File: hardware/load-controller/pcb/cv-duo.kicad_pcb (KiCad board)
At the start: 2 copper layers, 77.8 x 60.4 mm, 43 parts, among them J1 USB-C 16P receptacle, J2 5V DC input, J3 Relay load out (mains), J4 Pulse output, K1 Omron G5Q-1A 5VDC, Q1 AO3400A, Q2 AO3400A, SW1 RESET tactile, SW2 BOOT tactile, U1 ESP32-C3-WROOM-02 (4MB), U2 AP2112K-3.3, U3 USBLC6-2SC6

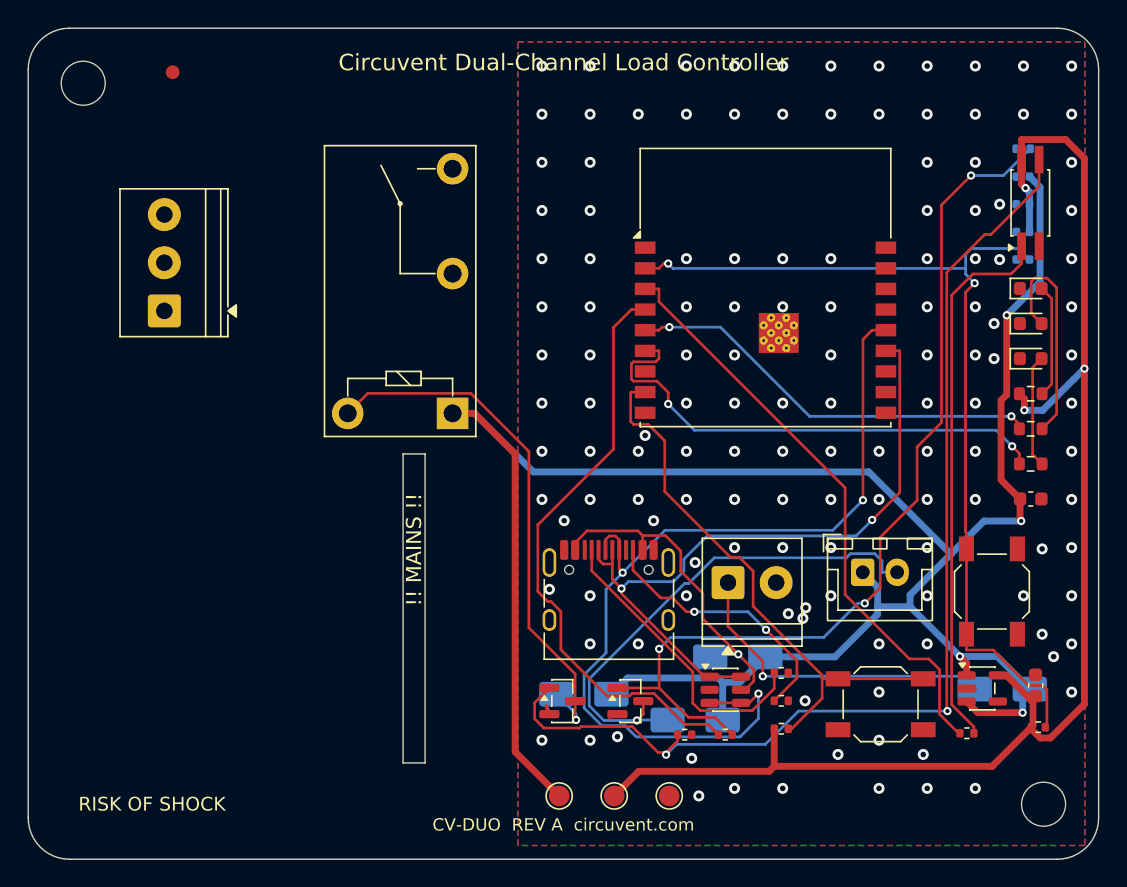
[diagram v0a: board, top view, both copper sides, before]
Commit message: Release 1.10.0, and stop shipping permissions the app never uses
Cut 1.10.0 (versionCode 12) and built it: AAB 38 MB, APK 83 MB, signed with the
upload key, JS bundle embedded.

Checking the generated manifest before writing the Play listing turned up
permissions no one had asked for. Every one of them is printed on the store page
for users to read before they install:

  RECORD_AUDIO          expo-camera asks for the microphone so video can be
                        recorded with sound. This app only ever puts the camera
                        in barcode mode to read a QR label, and expo-speech is
                        output-only - it speaks, it does not listen. Left in,
                        Play lists "Microphone" against a home-control app,
                        which is alarming, unexplainable and untrue.
  SYSTEM_ALERT_WINDOW   React Native's development overlay, useless in a release
                        build and shown to users as "Display over other apps".
  READ/WRITE_EXTERNAL_STORAGE
                        Legacy storage access nothing here touches.

Stripped via android.blockedPermissions. That emits tools:node="remove", which
is a merge instruction rather than a guarantee, so it was checked against the
finished artifact with aapt2 rather than the source manifest - all four are
absent from the APK.

NEARBY_WIFI_DEVICES now carries neverForLocation. Android otherwise treats it as
location-capable, because knowing which networks are in range is enough to place
someone, and Play's data safety review treats it the same way. The app uses it
only to join a new device's setup hotspot. That flag is a promise, so the plugin
says plainly that it has to come off if scan results are ever used positionally.

What is left is defensible: location for Wi-Fi onboarding (Android requires it),
camera for the QR label, nearby-devices flagged as non-positional.

Added mobile/store/listing with the text Play asks for - title, short and full
descriptions, and what'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
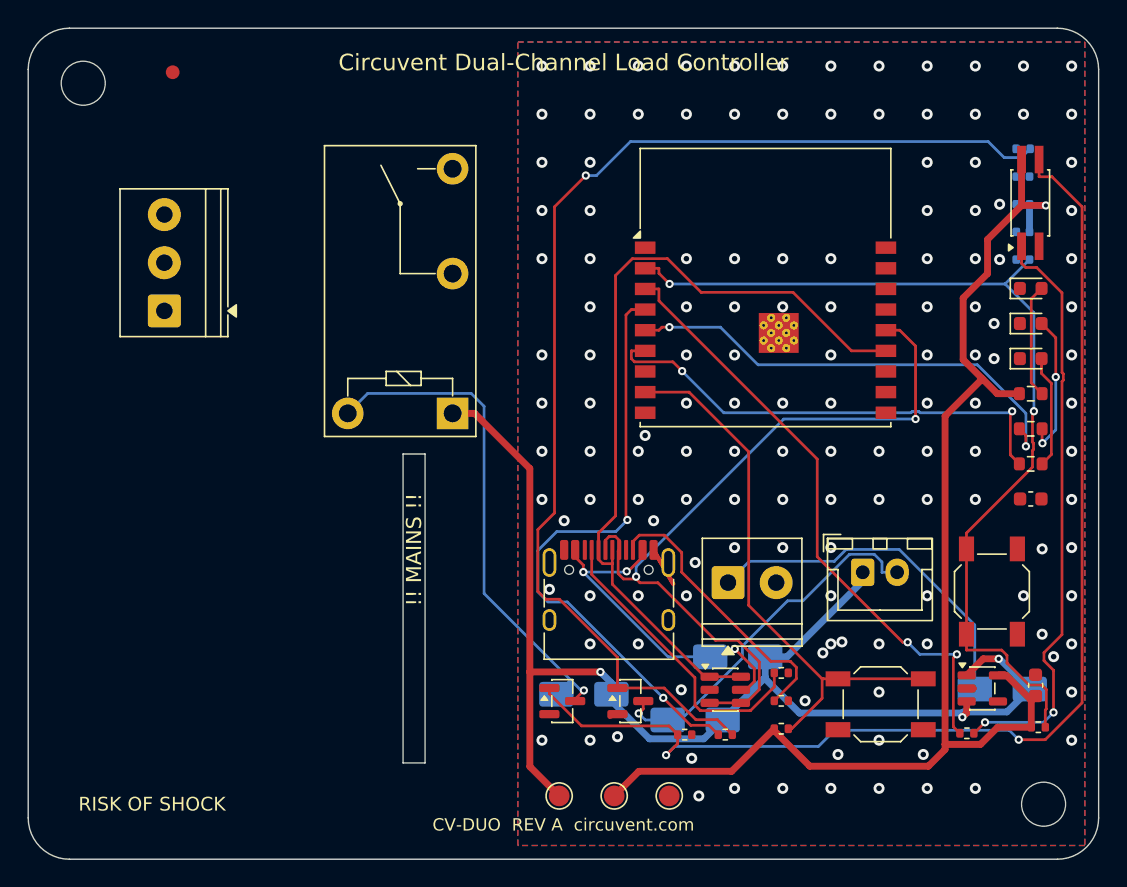
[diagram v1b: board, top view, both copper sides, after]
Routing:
- net +5V: track 160.4 -> 93.8 mm, vias 4 -> 3
- net PULSE_GATE: track 68.3 -> 85.5 mm, vias 3 -> 1
- net USB_D_P: track 68.5 -> 56.9 mm, vias 3 -> 2
- net PULSE_OUT: track 36.9 -> 26.5 mm
- net +3V3: track 104.8 -> 94.6 mm, vias 3 -> 1
- net USB_D_N: track 51.4 -> 59.8 mm, vias 2 -> 0
- net RELAY_GATE: track 80.1 -> 86.5 mm
- net RELAY_LED_A: track 16.3 -> 10.6 mm, vias 0 -> 2
- net GND: track 1.80 -> 6.90 mm, vias 137 -> 140
- net RELAY_LED: track 30.5 -> 34.2 mm
- net RELAY_OPT: track 39.8 -> 42.9 mm, vias 0 -> 2
- net VIN_EXT: track 23.6 -> 25.9 mm, vias 1 -> 0
- net RELAY_COIL: track 38.9 -> 37.2 mm
- net PULSE_LED: track 36.5 -> 35.2 mm
- net EN: track 67.9 -> 69.0 mm
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
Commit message: hardware: in-house 230VAC to 5V/3V3 isolated flyback to replace the HLK module
Twelve boards buy a Hi-Link HLK-PM03 and then spend an AMS1117 getting 3.3 V
out of it. This adds psu-5v3v3: a TNY274 flyback with opto/TL431 feedback that
produces both rails, so the host board drops its LDO and we stop depending on
one vendor for the part that makes everything else work.

New in the generator:

- hardware/lib/Circuvent.pretty, a repo-local footprint library, because KiCad
  ships no flyback bobbin and no safety-capacitor land. load_fp() prefers it
  over the KiCad install so a clean checkout rebuilds. The footprints are
  generated by make_lib.py, where every dimension is a named constant - the
  EE13 bobbin is a de facto standard rather than a controlled one, so that
  file is where you reconcile it with whoever winds the transformer.
- build_netlist_psu(), because a PSU has no MCU and the existing builder is
  organised around one.
- An HVDC netclass. Marking the whole primary as MAINS is correct about the
  hazard and wrong about the current: it forced 1.5 mm track and 2.0 mm
  clearance onto the BYPASS decoupling, and 33 of 33 primary nets failed to
  route. HVDC keeps a mains-grade gap to SELV and a sane one to itself.
- That split then broke reinforced_mains_to_selv, which excluded only MAINS
  and so began demanding 8 mm between AC_N and HV+ - two nets on the same side
  of the barrier, inside the same island. The two hazardous classes are now
  exempt from each other and both 8 mm from everything else.

Review found three defects in my own RCD clamp before it was committed: the
catch diode returned to the rail instead of catching at the drain, leaving the
leakage spike nowhere to go; the two snubber resistors were wired in parallel,
which halves the resistance instead of sharing the 325 V; and a decoupling cap
was orphaned.

The board is NOT fabricable as generated and the file says so. Thirteen
clearance errors remain, all primary copper against the optocoupler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
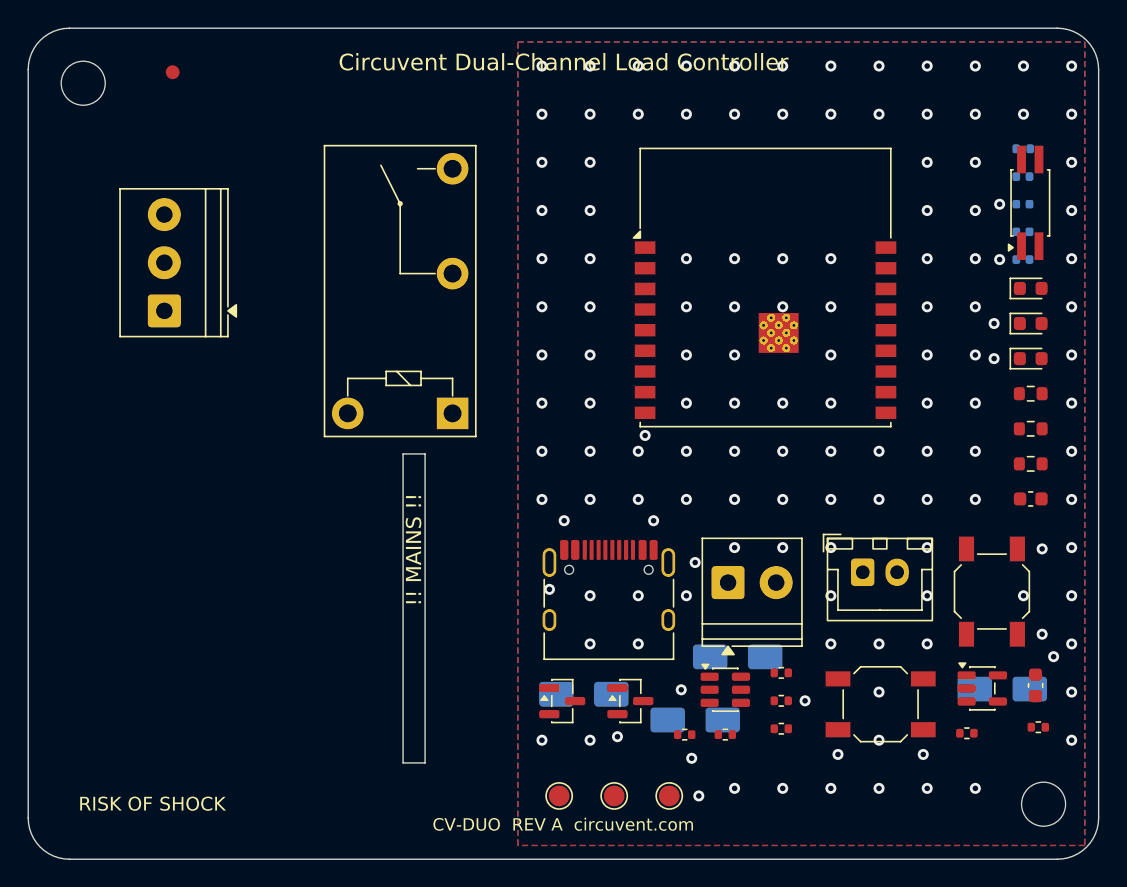
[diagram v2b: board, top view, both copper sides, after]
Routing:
- net +3V3: track 94.6 -> 0.00 mm, vias 1 -> 0
- net +5V: track 93.8 -> 0.00 mm, vias 3 -> 0
- net RELAY_GATE: track 86.5 -> 0.00 mm, vias 2 -> 0
- net PULSE_GATE: track 85.5 -> 0.00 mm, vias 1 -> 0
- net EN: track 69.0 -> 0.00 mm, vias 2 -> 0
- net USB_D_N: track 59.8 -> 0.00 mm
- net USB_D_P: track 56.9 -> 0.00 mm, vias 2 -> 0
- net RELAY_CTL: track 44.4 -> 0.00 mm, vias 2 -> 0
- net PULSE_PWM: track 44.3 -> 0.00 mm, vias 2 -> 0
- net RELAY_OPT: track 42.9 -> 0.00 mm, vias 2 -> 0
- net BOOT_N: track 40.2 -> 0.00 mm
- net RELAY_COIL: track 37.2 -> 0.00 mm, vias 1 -> 0
- net PULSE_LED: track 35.2 -> 0.00 mm, vias 2 -> 0
- net RELAY_LED: track 34.2 -> 0.00 mm, vias 2 -> 0
- net PULSE_OUT: track 26.5 -> 0.00 mm, vias 1 -> 0
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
